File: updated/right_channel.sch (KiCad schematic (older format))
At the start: 20 parts, among them J4 Left 0 ohms, J5 Right 8 ohms, J6 Conn_Coaxial, T3 AudioTxfmr

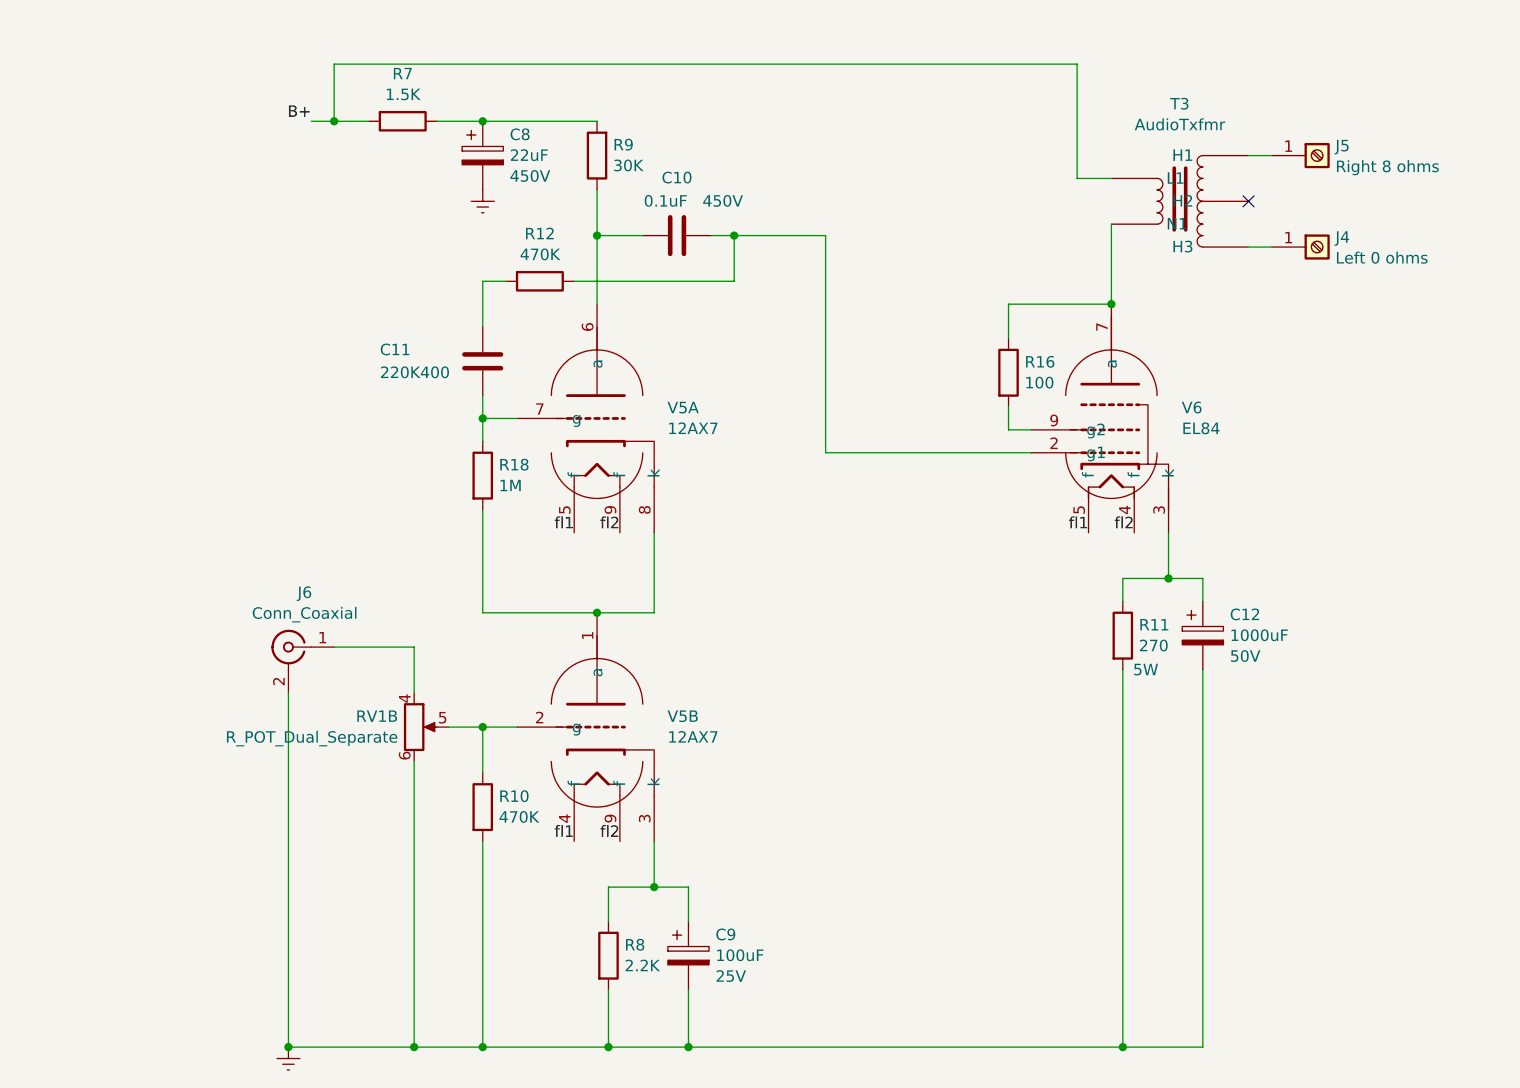
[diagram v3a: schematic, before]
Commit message: adding some components to try to stop a high pitch squal sound I sometimes hear from the amp
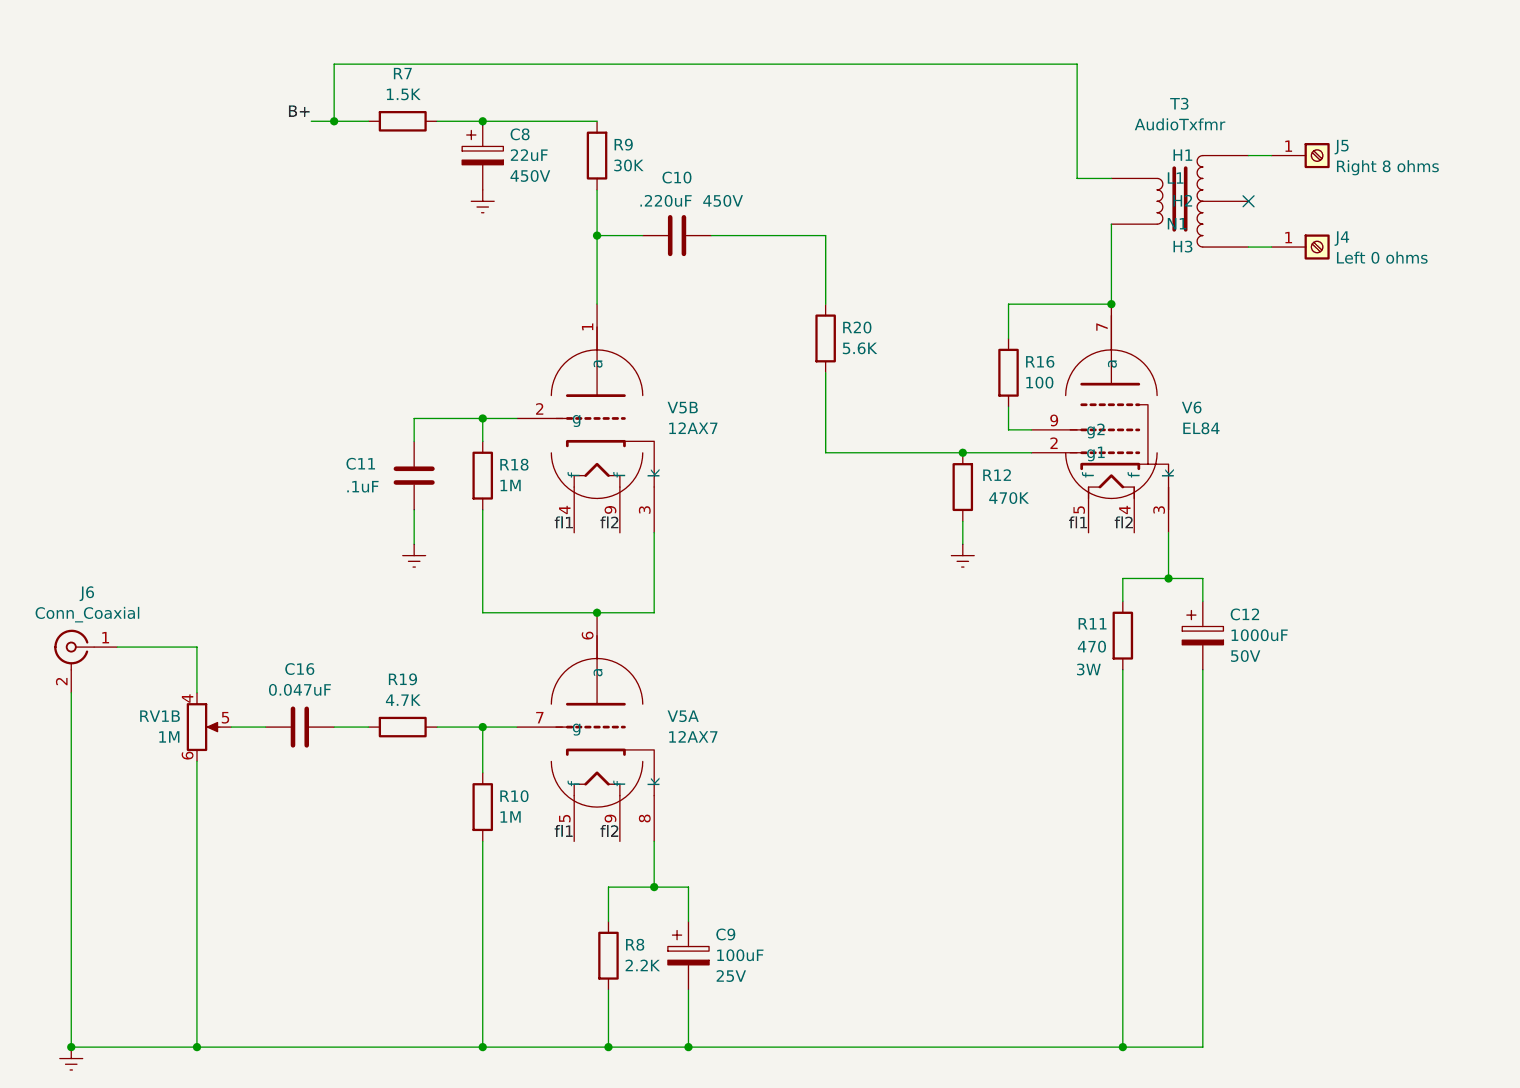
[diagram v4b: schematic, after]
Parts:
- added C16: 0.047uF, symbol Device:C
- added R19: 4.7K, symbol Device:R
- added R20: 5.6K, symbol Device:R
- C10: value 0.1uF -> .220uF
- C11: value 220K400 -> .1uF
- R10: value 470K -> 1M
- R11: value 270 -> 470; Power 5W -> 3W
- RV1: value R_POT_Dual_Separate -> 1M
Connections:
- net Earth: now also C11.2, R12.1
- net at C10.2, R9.1: now also V5.1 (a); no longer V5.6 (a)
- net at R12.2: now also V6.2 (g1), R20.2; no longer C11.1
- net at C9.1, R8.1: now also V5.8 (k); no longer V5.3 (k)
- new net: C10.1, R20.1
- new net: C11.1, R18.1, V5.2 (g)
- new net: R18.2, V5.3 (k), V5.6 (a)
- new net: R10.1, R19.1, V5.7 (g)
- new net: C16.2, RV1.5
- new net: C16.1, R19.2
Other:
- moved on the sheet: C11, J6, R12, RV1B, V5A, V5B
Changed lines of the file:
@@
 $Descr A4 11693 8268
 encoding utf-8
-Sheet 4 5
+Sheet 4 4
 Title ""
 Date ""
@@
 AR Path="/5F200EB9/5F20DF89" Ref="C10"  Part="1"
 F 0 "C10" V 4798 2200 50  0000 C CNN
-F 1 "0.1uF" V 4900 2150 50  0000 C CNN
+F 1 ".220uF" V 4900 2150 50  0000 C CNN
 F 2 "Capacitor_THT:CP_Radial_D4.0mm_P2.00mm" H 5088 2050 50  0001 C CNN
 F 3 "~" H 5050 2200 50  0001 C CNN
@@
 	4900 2200 4700 2200
 $Comp
-L Device:R R?
-U 1 1 5F20DF90
-P 4450 2400
-AR Path="/5F20DF90" Ref="R?"  Part="1"
-AR Path="/5F1F04D2/5F20DF90" Ref="R?"  Part="1"
-AR Path="/5F200EB9/5F20DF90" Ref="R12"  Part="1"
-F 0 "R12" V 4243 2400 50  0000 C CNN
-F 1 "470K" V 4334 2400 50  0000 C CNN
-F 2 "Resistor_THT:R_Axial_DIN0516_L15.5mm_D5.0mm_P20.32mm_Horizontal" V 4380 2400 50  0001 C CNN
-F 3 "~" H 4450 2400 50  0001 C CNN
-	1    4450 2400
-	0    1    1    0
-$EndComp
-$Comp
 L Device:C C?
 U 1 1 5F20DF96
-P 4200 2750
+P 3900 3250
 AR Path="/5F20DF96" Ref="C?"  Part="1"
 AR Path="/5F1F04D2/5F20DF96" Ref="C?"  Part="1"
 AR Path="/5F200EB9/5F20DF96" Ref="C11"  Part="1"
-F 0 "C11" H 3750 2800 50  0000 L CNN
-F 1 "220K400" H 3750 2700 50  0000 L CNN
-F 2 "Capacitor_THT:CP_Radial_D4.0mm_P2.00mm" H 4238 2600 50  0001 C CNN
-F 3 "~" H 4200 2750 50  0001 C CNN
-	1    4200 2750
+F 0 "C11" H 3600 3300 50  0000 L CNN
+F 1 ".1uF" H 3600 3200 50  0000 L CNN
+F 2 "Capacitor_THT:CP_Radial_D4.0mm_P2.00mm" H 3938 3100 50  0001 C CNN
+F 3 "~" H 3900 3250 50  0001 C CNN
+	1    3900 3250
 	1    0    0    -1
 $EndComp
@@
 L Connector:Conn_Coaxial J?
 U 1 1 5F20DFAC
-P 3350 4000
+P 2400 4000
 AR Path="/5F20DFAC" Ref="J?"  Part="1"
 AR Path="/5F1F04D2/5F20DFAC" Ref="J?"  Part="1"
 AR Path="/5F200EB9/5F20DFAC" Ref="J6"  Part="1"
-F 0 "J6" H 3278 4238 50  0000 C CNN
-F 1 "Conn_Coaxial" H 3278 4147 50  0000 C CNN
-F 2 "" H 3350 4000 50  0001 C CNN
-F 3 " ~" H 3350 4000 50  0001 C CNN
-	1    3350 4000
+F 0 "J6" H 2328 4238 50  0000 C CNN
+F 1 "Conn_Coaxial" H 2328 4147 50  0000 C CNN
+F 2 "" H 2400 4000 50  0001 C CNN
+F 3 " ~" H 2400 4000 50  0001 C CNN
+	1    2400 4000
 	-1   0    0    -1
 $EndComp
 Wire Wire Line
-	3900 4500 3900 5750
-Wire Wire Line
-	3900 5750 3350 5750
-Wire Wire Line
-	3350 5750 3350 4200
+	2950 4500 2950 5750
+Wire Wire Line
+	2950 5750 2400 5750
+Wire Wire Line
+	2400 5750 2400 4200
 $Comp
 L power:Earth #PWR?
 U 1 1 5F20DFBB
-P 3350 5750
+P 2400 5750
 AR Path="/5F20DFBB" Ref="#PWR?"  Part="1"
 AR Path="/5F1F04D2/5F20DFBB" Ref="#PWR?"  Part="1"
 AR Path="/5F200EB9/5F20DFBB" Ref="#PWR08"  Part="1"
-F 0 "#PWR08" H 3350 5500 50  0001 C CNN
-F 1 "Earth" H 3350 5600 50  0001 C CNN
-F 2 "" H 3350 5750 50  0001 C CNN
-F 3 "~" H 3350 5750 50  0001 C CNN
-	1    3350 5750
-	1    0    0    -1
-$EndComp
-Connection ~ 3350 5750
-Wire Wire Line
-	3550 4000 3900 4000
-Wire Wire Line
-	3900 4000 3900 4200
-Wire Wire Line
-	4050 4350 4200 4350
+F 0 "#PWR08" H 2400 5500 50  0001 C CNN
+F 1 "Earth" H 2400 5600 50  0001 C CNN
+F 2 "" H 2400 5750 50  0001 C CNN
+F 3 "~" H 2400 5750 50  0001 C CNN
+	1    2400 5750
+	1    0    0    -1
+$EndComp
+Connection ~ 2400 5750
+Wire Wire Line
+	2600 4000 2950 4000
+Wire Wire Line
+	2950 4000 2950 4200
+Wire Wire Line
+	3100 4350 3250 4350
 Text Label 4600 3500 2    50   ~ 0
 fl1
@@
 AR Path="/5F200EB9/5F20DFC9" Ref="R10"  Part="1"
 F 0 "R10" H 4270 4746 50  0000 L CNN
-F 1 "470K" H 4270 4655 50  0000 L CNN
+F 1 "1M" H 4270 4655 50  0000 L CNN
 F 2 "Resistor_THT:R_Axial_DIN0516_L15.5mm_D5.0mm_P20.32mm_Horizontal" V 4130 4700 50  0001 C CNN
 F 3 "~" H 4200 4700 50  0001 C CNN
@@
 Wire Wire Line
 	4200 4550 4200 4350
-Connection ~ 4200 4350
 Wire Wire Line
 	4200 4350 4350 4350
@@
 $EndComp
 Wire Wire Line
-	4200 5750 3900 5750
+	4200 5750 2950 5750
 Wire Wire Line
 	4200 4850 4200 5750
-Connection ~ 3900 5750
-Connection ~ 4200 5750
+Connection ~ 2950 5750
 Wire Wire Line
 	5100 5500 5100 5750
@@
 	4750 5750 5100 5750
 Wire Wire Line
-	4200 2900 4200 3000
-Wire Wire Line
 	4350 3000 4200 3000
-Connection ~ 4200 3000
 Wire Wire Line
 	4200 3000 4200 3100
-Wire Wire Line
-	5200 2200 5300 2200
-Wire Wire Line
-	4300 2400 4200 2400
-Wire Wire Line
-	4200 2400 4200 2600
-Wire Wire Line
-	4600 2400 5300 2400
-Wire Wire Line
-	5300 2400 5300 2200
-Connection ~ 5300 2200
-Wire Wire Line
-	5300 2200 5700 2200
 NoConn ~ 7550 2050
 $Comp
@@
 	7650 1850 7550 1850
 Wire Wire Line
-	6600 3150 5700 3150
-Wire Wire Line
-	5700 3150 5700 2200
+	6600 3150 6300 3150
 Text Label 6850 3500 2    50   ~ 0
 fl1
@@
 L local:12AX7 V5
 U 1 1 5F225712
+P 4700 4300
+F 0 "V5" H 5008 4296 50  0000 L CNN
+F 1 "12AX7" H 5008 4205 50  0000 L CNN
+F 2 "Valve:Valve_ECC-83-1" H 4720 4300 50  0001 C CNN
+F 3 "" H 4720 4300 50  0001 C CNN
+	1    4700 4300
+	1    0    0    -1
+$EndComp
+$Comp
+L local:12AX7 V5
+U 2 1 5F22A5F0
 P 4700 2950
 F 0 "V5" H 5008 2946 50  0000 L CNN
@@
 F 2 "Valve:Valve_ECC-83-1" H 4720 2950 50  0001 C CNN
 F 3 "" H 4720 2950 50  0001 C CNN
-	1    4700 2950
-	1    0    0    -1
-$EndComp
-$Comp
-L local:12AX7 V5
-U 2 1 5F22A5F0
-P 4700 4300
-F 0 "V5" H 5008 4296 50  0000 L CNN
-F 1 "12AX7" H 5008 4205 50  0000 L CNN
-F 2 "Valve:Valve_ECC-83-1" H 4720 4300 50  0001 C CNN
-F 3 "" H 4720 4300 50  0001 C CNN
-	2    4700 4300
+	2    4700 2950
 	1    0    0    -1
 $EndComp
@@
 L Device:R_POT_Dual_Separate RV1
 U 2 1 5F245DA2
-P 3900 4350
-F 0 "RV1" H 3830 4396 50  0000 R CNN
-F 1 "R_POT_Dual_Separate" H 3830 4305 50  0000 R CNN
-F 2 "" H 3900 4350 50  0001 C CNN
-F 3 "~" H 3900 4350 50  0001 C CNN
-	2    3900 4350
+P 2950 4350
+F 0 "RV1" H 2880 4396 50  0000 R CNN
+F 1 "1M" H 2880 4305 50  0000 R CNN
+F 2 "" H 2950 4350 50  0001 C CNN
+F 3 "~" H 2950 4350 50  0001 C CNN
+	2    2950 4350
 	1    0    0    -1
 $EndComp
@@
 AR Path="/5F1F04D2/5F20E02D" Ref="R?"  Part="1"
 AR Path="/5F200EB9/5F20E02D" Ref="R11"  Part="1"
-F 0 "R11" H 7070 3996 50  0000 L CNN
-F 1 "270" H 7070 3905 50  0000 L CNN
+F 0 "R11" H 6800 4000 50  0000 L CNN
+F 1 "470" H 6800 3900 50  0000 L CNN
 F 2 "Resistor_THT:R_Axial_DIN0516_L15.5mm_D5.0mm_P20.32mm_Horizontal" V 6930 3950 50  0001 C CNN
 F 3 "~" H 7000 3950 50  0001 C CNN
-F 4 "5W" H 7100 3800 50  0000 C CNN "Power"
+F 4 "3W" H 6850 3800 50  0000 C CNN "Power"
 	1    7000 3950
 	1    0    0    -1
 $EndComp
+$Comp
+L Device:R R?
+U 1 1 5F20DF90
+P 6300 3300
+AR Path="/5F20DF90" Ref="R?"  Part="1"
+AR Path="/5F1F04D2/5F20DF90" Ref="R?"  Part="1"
+AR Path="/5F200EB9/5F20DF90" Ref="R12"  Part="1"
+F 0 "R12" H 6150 3250 50  0000 C CNN
+F 1 "470K" H 6100 3350 50  0000 C CNN
+F 2 "Resistor_THT:R_Axial_DIN0516_L15.5mm_D5.0mm_P20.32mm_Horizontal" V 6230 3300 50  0001 C CNN
+F 3 "~" H 6300 3300 50  0001 C CNN
+	1    6300 3300
+	-1   0    0    1
+$EndComp
+Connection ~ 6300 3150
+Wire Wire Line
+	6300 3150 5700 3150
+$Comp
+L power:Earth #PWR013
+U 1 1 5F557E01
+P 6300 3550
+F 0 "#PWR013" H 6300 3300 50  0001 C CNN
+F 1 "Earth" H 6300 3400 50  0001 C CNN
+F 2 "" H 6300 3550 50  0001 C CNN
+F 3 "~" H 6300 3550 50  0001 C CNN
+	1    6300 3550
+	1    0    0    -1
+$EndComp
+Wire Wire Line
+	6300 3550 6300 3450
+Wire Wire Line
+	5200 2200 5700 2200
+Wire Wire Line
+	4200 3000 3900 3000
+Wire Wire Line
+	3900 3000 3900 3100
+Connection ~ 4200 3000
+$Comp
+L power:Earth #PWR012
+U 1 1 5F561B8E
+P 3900 3550
+F 0 "#PWR012" H 3900 3300 50  0001 C CNN
+F 1 "Earth" H 3900 3400 50  0001 C CNN
+F 2 "" H 3900 3550 50  0001 C CNN
+F 3 "~" H 3900 3550 50  0001 C CNN
+	1    3900 3550
+	1    0    0    -1
+$EndComp
+Wire Wire Line
+	3900 3550 3900 3400
+$Comp
+L Device:R R20
+U 1 1 5F56722A
+P 5700 2650
+F 0 "R20" H 5770 2696 50  0000 L CNN
+F 1 "5.6K" H 5770 2605 50  0000 L CNN
+F 2 "" V 5630 2650 50  0001 C CNN
+F 3 "~" H 5700 2650 50  0001 C CNN
+	1    5700 2650
+	1    0    0    -1
+$EndComp
+Wire Wire Line
+	5700 2500 5700 2200
+Wire Wire Line
+	5700 2800 5700 3150
+$Comp
+L Device:C C16
+U 1 1 5F5768EB
+P 3400 4350
+F 0 "C16" V 3148 4350 50  0000 C CNN
+F 1 "0.047uF" V 3239 4350 50  0000 C CNN
+F 2 "" H 3438 4200 50  0001 C CNN
+F 3 "~" H 3400 4350 50  0001 C CNN
+	1    3400 4350
+	0    1    1    0
+$EndComp
+$Comp
+L Device:R R19
+U 1 1 5F5828D1
+P 3850 4350
+F 0 "R19" V 3643 4350 50  0000 C CNN
+F 1 "4.7K" V 3734 4350 50  0000 C CNN
+F 2 "" V 3780 4350 50  0001 C CNN
+F 3 "~" H 3850 4350 50  0001 C CNN
+	1    3850 4350
+	0    1    1    0
+$EndComp
+Wire Wire Line
+	3550 4350 3700 4350
+Wire Wire Line
+	4000 4350 4200 4350
+Connection ~ 4200 4350
+Connection ~ 4200 5750
 $EndSCHEMATC

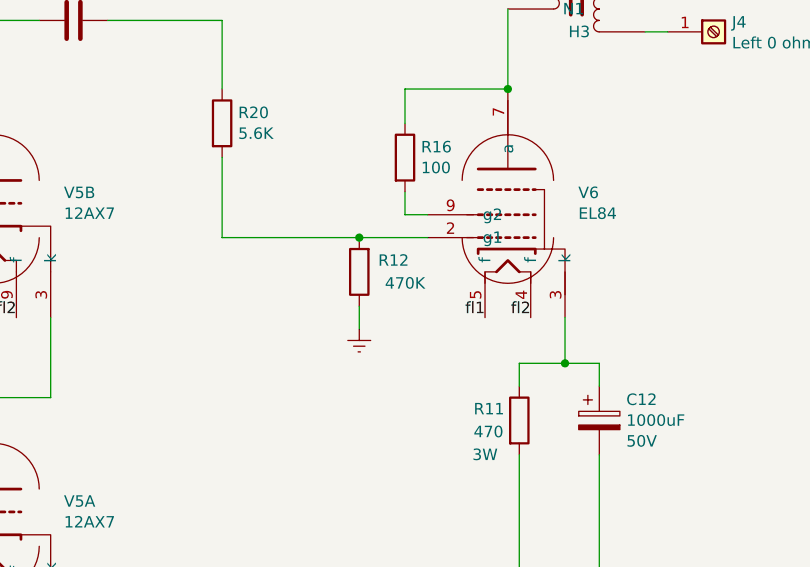
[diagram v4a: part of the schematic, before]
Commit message: change EL84 grid leak resistor to 1M
In the day time, I sort of feel the amp is too quiet. That adding the 5.6k resistor inline has reduced the signal. This small resistance divide is like 98% the input. But that is still the 2% loss of signal. I think the gain stage of these preamp tubes is not very strong. And I read the EL84 does have a wider response to small changes in input impedance.
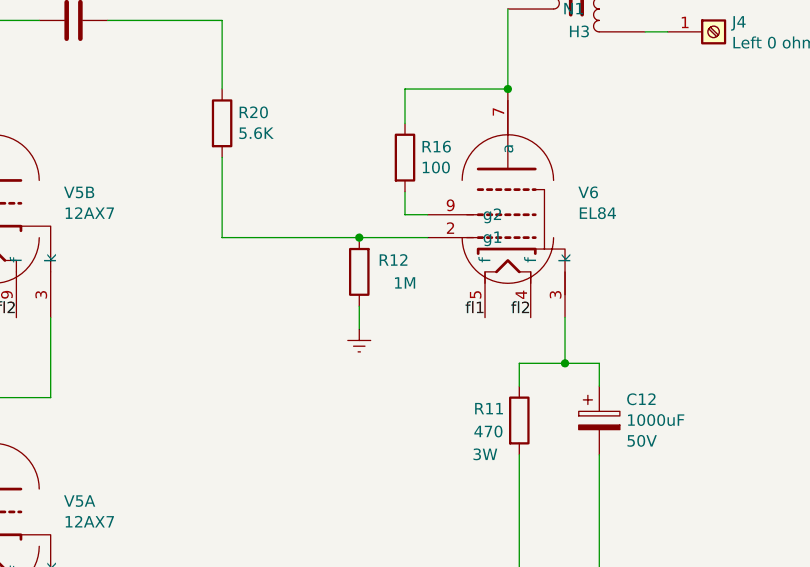
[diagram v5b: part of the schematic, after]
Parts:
- R12: value 470K -> 1M
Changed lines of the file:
@@
 AR Path="/5F200EB9/5F20DF90" Ref="R12"  Part="1"
 F 0 "R12" H 6150 3250 50  0000 C CNN
-F 1 "470K" H 6100 3350 50  0000 C CNN
+F 1 "1M" H 6100 3350 50  0000 C CNN
 F 2 "Resistor_THT:R_Axial_DIN0516_L15.5mm_D5.0mm_P20.32mm_Horizontal" V 6230 3300 50  0001 C CNN
 F 3 "~" H 6300 3300 50  0001 C CNN

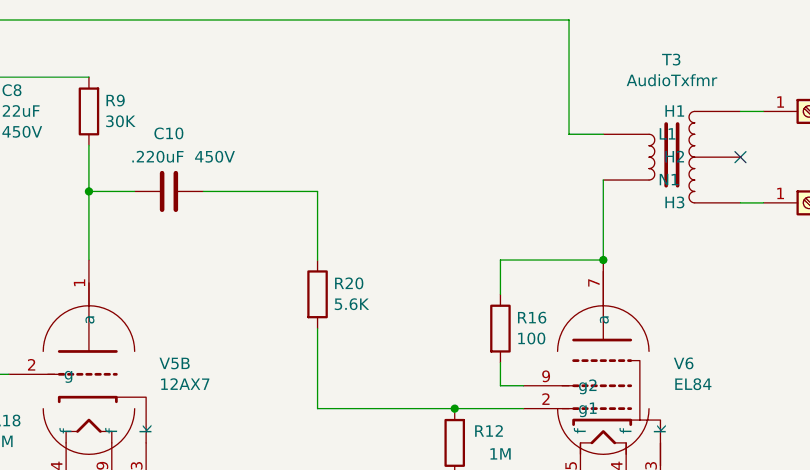
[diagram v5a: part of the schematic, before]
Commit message: install vfd spectrograph
upgrade preamp tubes to use shielded sockets.
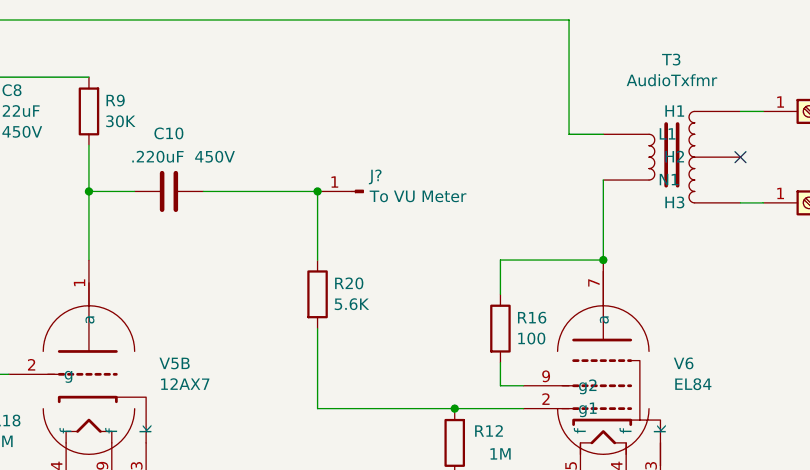
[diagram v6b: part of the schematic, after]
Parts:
- added J?: To VU Meter, symbol Connector:Conn_01x01_Male
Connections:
- net at C10.1, R20.1: now also J?.1 (Pin_1)
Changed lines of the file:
@@
 Connection ~ 4200 4350
 Connection ~ 4200 5750
+$Comp
+L Connector:Conn_01x01_Male J?
+U 1 1 5F53FDB2
+P 5900 2200
+AR Path="/5F1F04D2/5F53FDB2" Ref="J?"  Part="1"
+AR Path="/5F200EB9/5F53FDB2" Ref="J?"  Part="1"
+F 0 "J?" H 5872 2132 50  0000 R CNN
+F 1 "To VU Meter" H 5872 2223 50  0000 R CNN
+F 2 "" H 5900 2200 50  0001 C CNN
+F 3 "~" H 5900 2200 50  0001 C CNN
+	1    5900 2200
+	-1   0    0    1
+$EndComp
+Connection ~ 5700 2200
 $EndSCHEMATC
